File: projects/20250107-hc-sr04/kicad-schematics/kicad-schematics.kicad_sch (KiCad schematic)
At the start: 6 parts, among them J1 HC SR04

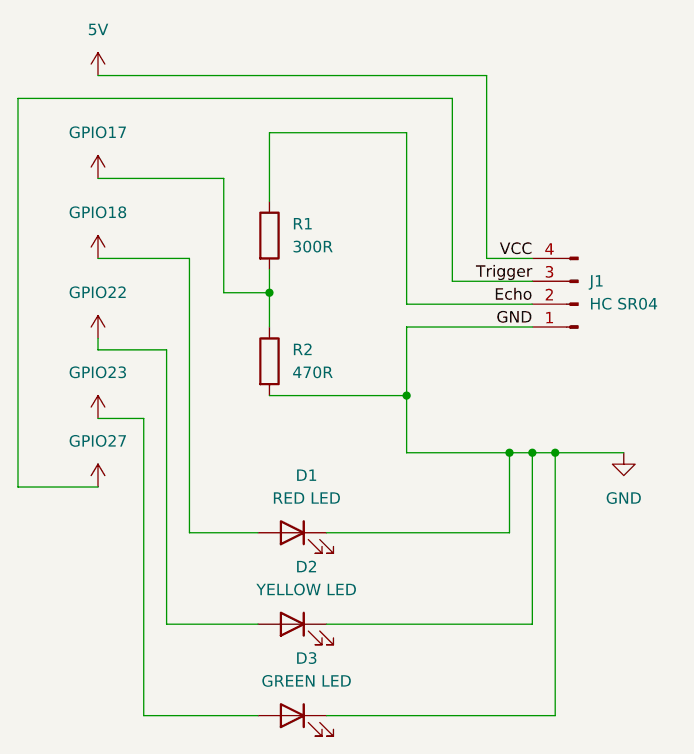
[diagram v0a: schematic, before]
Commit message: ➕ Finalizing the HC-SR04 Project (Correct Schemas)
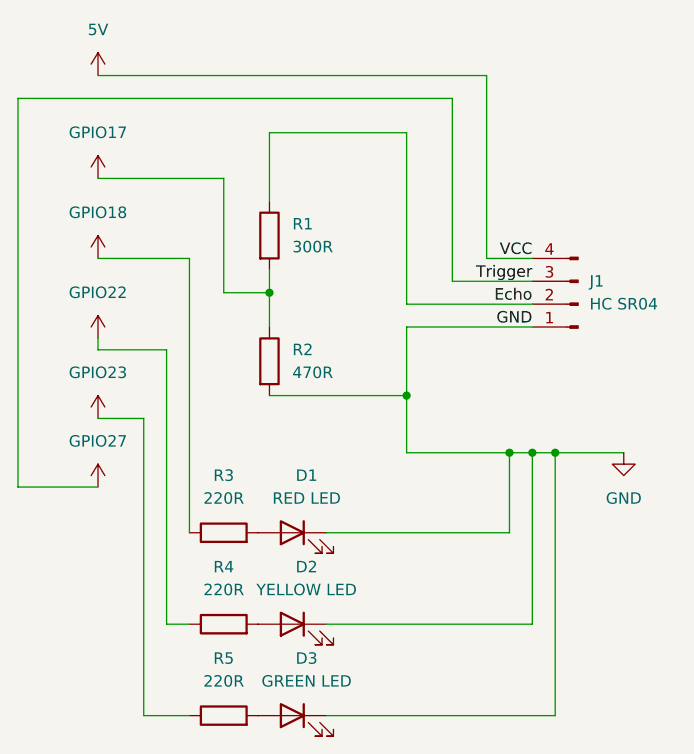
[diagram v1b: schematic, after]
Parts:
- added R3, R4, R5: 220R, symbol Device:R
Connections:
- net GPIO18: now also R3.1; no longer D1.2 (A)
- net GPIO22: now also R4.1; no longer D2.2 (A)
- net GPIO23: now also R5.1; no longer D3.2 (A)
- new net: D3.2 (A), R5.2
- new net: D1.2 (A), R3.2
- new net: D2.2 (A), R4.2
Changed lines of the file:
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@@
-	(wire
-		(pts
-			(xy 43.18 73.66) (xy 50.8 73.66)
-		)
-		(stroke
-			(width 0)
-			(type default)
-		)
-	)
-	(wire
-		(pts
-			(xy 50.8 83.82) (xy 40.64 83.82)
-		)
-		(stroke
-			(width 0)
-			(type default)
-		)
-	)
 	(wire
 		(pts
@@
 	(wire
 		(pts
-			(xy 38.1 93.98) (xy 50.8 93.98)
-		)
-		(stroke
-			(width 0)
-			(type default)
-		)
-	)
-	(wire
-		(pts
 			(xy 67.31 64.77) (xy 78.74 64.77)
 		)
@@
 	(wire
 		(pts
+			(xy 38.1 93.98) (xy 43.18 93.98)
+		)
+		(stroke
+			(width 0)
+			(type default)
+		)
+	)
+	(wire
+		(pts
 			(xy 78.74 64.77) (xy 81.28 64.77)
 		)
@@
 		(pts
 			(xy 67.31 58.42) (xy 67.31 64.77)
+		)
+		(stroke
+			(width 0)
+			(type default)
+		)
+	)
+	(wire
+		(pts
+			(xy 40.64 83.82) (xy 43.18 83.82)
 		)
 		(stroke
@@
 	)
 	(symbol
+		(lib_id "Device:R")
+		(at 46.99 93.98 90)
+		(unit 1)
+		(exclude_from_sim no)
+		(in_bom yes)
+		(on_board yes)
+		(dnp no)
+		(fields_autoplaced yes)
+		(property "Reference" "R5"
+			(at 46.99 87.63 90)
+			(effects
+				(font
+					(size 1.27 1.27)
+				)
+			)
+		)
+		(property "Value" "220R"
+			(at 46.99 90.17 90)
+			(effects
+				(font
+					(size 1.27 1.27)
+				)
+			)
+		)
+		(property "Footprint" ""
+			(at 46.99 95.758 90)
+			(effects
+				(font
+					(size 1.27 1.27)
+				)
+				(hide yes)
+			)
+		)
+		(property "Datasheet" "~"
+			(at 46.99 93.98 0)
+			(effects
+				(font
+					(size 1.27 1.27)
+				)
+				(hide yes)
+			)
+		)
+		(property "Description" "Resistor"
+			(at 46.99 93.98 0)
+			(effects
+				(font
+					(size 1.27 1.27)
+				)
+				(hide yes)
+			)
+		)
+		(pin "1"
+		)
+		(pin "2"
+		)
+		(instances
+			(project "kicad-schematics"
+				(path "/da9d2162-13b0-4dac-8690-f1863504d128"
+					(reference "R5")
+					(unit 1)
+				)
+			)
+		)
+	)
+	(symbol
 		(lib_id "Device:LED")
 		(at 54.61 73.66 0)
@@
 	)
 	(symbol
+		(lib_id "Device:R")
+		(at 46.99 83.82 90)
+		(unit 1)
+		(exclude_from_sim no)
+		(in_bom yes)
+		(on_board yes)
+		(dnp no)
+		(fields_autoplaced yes)
+		(property "Reference" "R4"
+			(at 46.99 77.47 90)
+			(effects
+				(font
+					(size 1.27 1.27)
+				)
+			)
+		)
+		(property "Value" "220R"
+			(at 46.99 80.01 90)
+			(effects
+				(font
+					(size 1.27 1.27)
+				)
+			)
+		)
+		(property "Footprint" ""
+			(at 46.99 85.598 90)
+			(effects
+				(font
+					(size 1.27 1.27)
+				)
+				(hide yes)
+			)
+		)
+		(property "Datasheet" "~"
+			(at 46.99 83.82 0)
+			(effects
+				(font
+					(size 1.27 1.27)
+				)
+				(hide yes)
+			)
+		)
+		(property "Description" "Resistor"
+			(at 46.99 83.82 0)
+			(effects
+				(font
+					(size 1.27 1.27)
+				)
+				(hide yes)
+			)
+		)
+		(pin "1"
+		)
+		(pin "2"
+		)
+		(instances
+			(project "kicad-schematics"
+				(path "/da9d2162-13b0-4dac-8690-f1863504d128"
+					(reference "R4")
+					(unit 1)
+				)
+			)
+		)
+	)
+	(symbol
 		(lib_id "power:VCC")
 		(at 33.02 60.96 0)
@@
 					(unit 1)
 				)
+			)
+		)
+	)
+	(symbol
+		(lib_id "Device:R")
+		(at 46.99 73.66 90)
+		(unit 1)
+		(exclude_from_sim no)
+		(in_bom yes)
+		(on_board yes)
+		(dnp no)
+		(fields_autoplaced yes)
+		(property "Reference" "R3"
+			(at 46.99 67.31 90)
+			(effects
+				(font
+					(size 1.27 1.27)
+				)
+			)
+		)
+		(property "Value" "220R"
+			(at 46.99 69.85 90)
+			(effects
+				(font
+					(size 1.27 1.27)
+				)
+			)
+		)
+		(property "Footprint" ""
+			(at 46.99 75.438 90)
+			(effects
+				(font
+					(size 1.27 1.27)
+				)
+				(hide yes)
+			)
+		)
+		(property "Datasheet" "~"
+			(at 46.99 73.66 0)
+			(effects
+				(font
+					(size 1.27 1.27)
+				)
+				(hide yes)
+			)
+		)
+		(property "Description" "Resistor"
+			(at 46.99 73.66 0)
+			(effects
+				(font
+					(size 1.27 1.27)
+				)
+				(hide yes)
+			)
+		)
+		(pin "1"
+		)
+		(pin "2"
+		)
+		(instances
+			(project ""
+				(path "/da9d2162-13b0-4dac-8690-f1863504d128"
+					(reference "R3")
+					(unit 1)
+				)
